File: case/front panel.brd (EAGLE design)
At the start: 165 x 30.1 mm, 3 parts

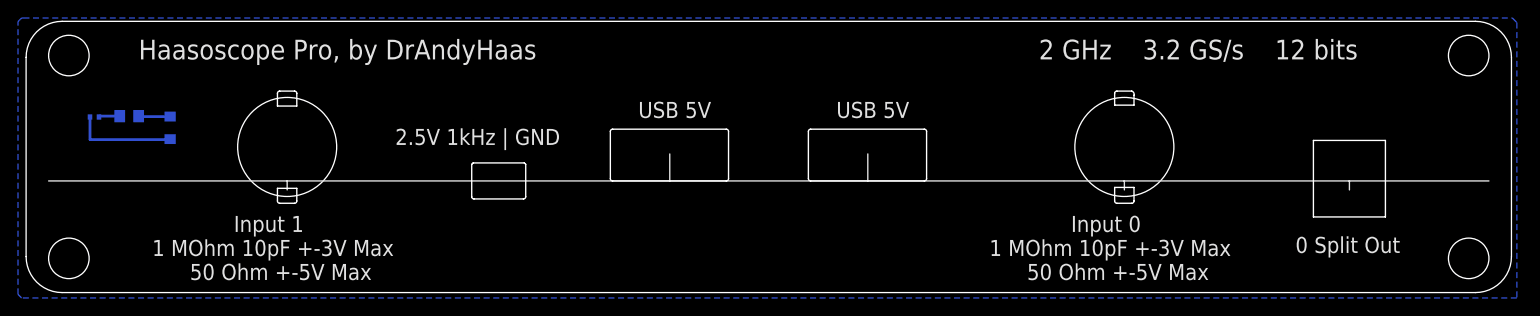
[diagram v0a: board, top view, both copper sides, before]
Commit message: add rgb leds
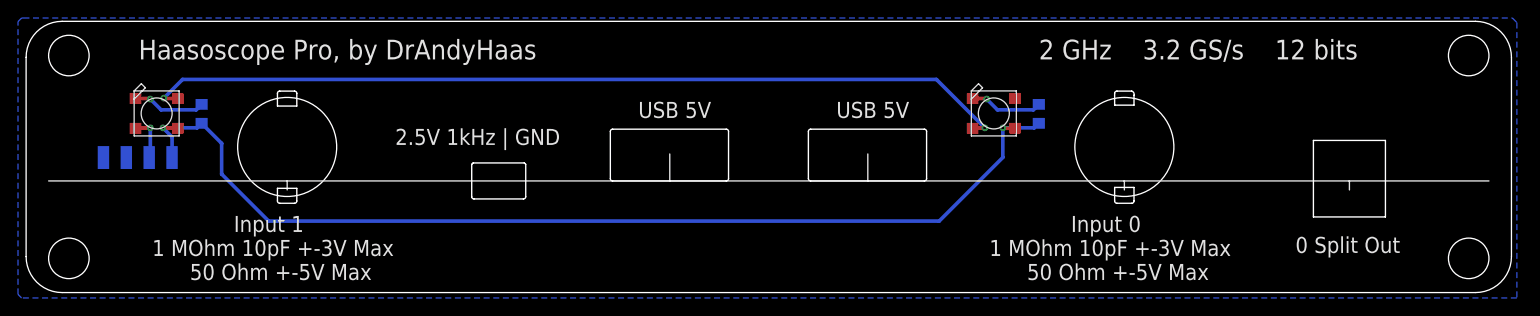
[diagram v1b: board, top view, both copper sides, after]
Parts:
- removed D2: green, MF_LEDs:LED0805
- removed R2: 3.3k, FlashPCB_Resistors:RES-0402
- added C2: 0.1uF, Nordic_nRF:RESC0805_N
- added CN1: 1X4SMT, adafruit:1X4-SMT
- added LED1, LED2: WS2812B_5050N, adafruit:WS2812B-NARROW
- C1: value 10uF -> 0.1uF
- moved C1 8.11 mm to (17.0, 20.0), turned to 90 degrees
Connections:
- new net DIN: CN1.2, LED1.4-DIN
- net 5V: now also C2.1, CN1.1, LED1.1-VDD, LED2.1-VDD; no longer D2.ANODE
- net GND: now also C2.2, CN1.3, CN1.4, LED1.3-GND, LED2.3-GND; no longer R2.P$1
- net N$2: now also LED1.2-DOUT, LED2.4-DIN; no longer D2.CATHODE, R2.P$2
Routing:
- net 5V: track 3.52 -> 117.2 mm, vias 0 -> 2
- net N$2: track 11.4 -> 97.2 mm, vias 0 -> 2
- net GND: track 2.34 -> 16.2 mm, vias 0 -> 2
- net DIN: track 0.00 -> 5.02 mm, vias 0 -> 1
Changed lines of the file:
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@@
 <drawing>
 <settings>
-<setting alwaysvectorfont="no"/>
+<setting alwaysvectorfont="yes"/>
 <setting verticaltext="up"/>
 </settings>
@@
 </autorouter>
 <elements>
-<element name="D2" library="MF_LEDs" package="LED0805" value="green" x="13.5" y="18.4" smashed="yes" rot="MR90">
-<attribute name="HOUSEPART" value="NO" x="19.9" y="15.4" size="1.778" layer="28" rot="MR90" display="off"/>
-<attribute name="MPN" value="" x="19.9" y="15.4" size="1.778" layer="28" rot="MR90" display="off"/>
-<attribute name="POPULATE" value="1" x="19.9" y="15.4" size="1.778" layer="28" rot="MR90" display="off"/>
-<attribute name="URL" value="" x="19.9" y="15.4" size="1.778" layer="28" rot="MR90" display="off"/>
-</element>
-<element name="R2" library="FlashPCB_Resistors" package="RES-0402" value="3.3k" x="5.1" y="19.6" smashed="yes" rot="MR0"/>
-<element name="C1" library="Nordic_nRF" library_urn="urn:adsk.eagle:library:169009" package="RESC0805_N" package3d_urn="urn:adsk.eagle:package:2593736/1" value="10uF" x="8.9" y="19.7" smashed="yes" rot="MR0"/>
+<element name="C1" library="Nordic_nRF" library_urn="urn:adsk.eagle:library:169009" package="RESC0805_N" package3d_urn="urn:adsk.eagle:package:2593736/1" value="0.1uF" x="17" y="20" smashed="yes" rot="MR90"/>
+<element name="LED1" library="adafruit" package="WS2812B-NARROW" value="WS2812B_5050N" x="12" y="20" smashed="yes"/>
+<element name="LED2" library="adafruit" package="WS2812B-NARROW" value="WS2812B_5050N" x="105" y="20" smashed="yes"/>
+<element name="CN1" library="adafruit" package="1X4-SMT" value="1X4SMT" x="9.9" y="15.1" smashed="yes" rot="MR0"/>
+<element name="C2" library="Nordic_nRF" library_urn="urn:adsk.eagle:library:169009" package="RESC0805_N" package3d_urn="urn:adsk.eagle:package:2593736/1" value="0.1uF" x="110" y="20" smashed="yes" rot="MR90"/>
 </elements>
 <signals>
@@
 </signal>
 <signal name="GND">
-<contactref element="R2" pad="P$1"/>
 <contactref element="C1" pad="2"/>
-<wire x1="7.9" y1="19.7" x2="5.7" y2="19.7" width="0.3048" layer="16"/>
-<wire x1="5.7" y1="19.7" x2="5.6" y2="19.6" width="0.3048" layer="16"/>
 <polygon width="0.1524" layer="16">
 <vertex x="-2.8" y="30.6"/>
@@
 <vertex x="-3" y="30.6"/>
 </polygon>
+<contactref element="LED1" pad="3-GND"/>
+<contactref element="LED2" pad="3-GND"/>
+<contactref element="CN1" pad="4"/>
+<contactref element="CN1" pad="3"/>
+<contactref element="C2" pad="2"/>
+<wire x1="102.65" y1="21.65" x2="104.15" y2="21.65" width="0.4064" layer="1"/>
+<wire x1="104.15" y1="21.65" x2="104.2" y2="21.6" width="0.4064" layer="1"/>
+<via x="104.2" y="21.6" extent="1-16" drill="0.35"/>
+<wire x1="109.4" y1="20.4" x2="105.4" y2="20.4" width="0.4064" layer="16"/>
+<wire x1="104.2" y1="21.6" x2="105.4" y2="20.4" width="0.4064" layer="16"/>
+<wire x1="110" y1="21" x2="109.4" y2="20.4" width="0.4064" layer="16"/>
+<wire x1="9.65" y1="21.65" x2="11.25" y2="21.65" width="0.4064" layer="1"/>
+<wire x1="11.25" y1="21.65" x2="11.3" y2="21.6" width="0.4064" layer="1"/>
+<via x="11.3" y="21.6" extent="1-16" drill="0.35"/>
+<wire x1="16.4" y1="20.4" x2="12.5" y2="20.4" width="0.4064" layer="16"/>
+<wire x1="11.3" y1="21.6" x2="12.5" y2="20.4" width="0.4064" layer="16"/>
+<wire x1="17" y1="21" x2="16.4" y2="20.4" width="0.4064" layer="16"/>
 </signal>
 <signal name="5V">
-<contactref element="D2" pad="ANODE"/>
 <contactref element="C1" pad="1"/>
-<wire x1="13.5" y1="19.65" x2="10.05" y2="19.65" width="0.3048" layer="16"/>
-<wire x1="10.05" y1="19.65" x2="10" y2="19.7" width="0.3048" layer="16"/>
+<contactref element="LED2" pad="1-VDD"/>
+<contactref element="LED1" pad="1-VDD"/>
+<contactref element="CN1" pad="1"/>
+<contactref element="C2" pad="1"/>
+<wire x1="14.35" y1="18.35" x2="14.3" y2="18.4" width="0.4064" layer="1"/>
+<wire x1="14.3" y1="18.4" x2="12.7" y2="18.4" width="0.4064" layer="1"/>
+<via x="12.7" y="18.4" extent="1-16" drill="0.35"/>
+<wire x1="12.7" y1="18.4" x2="13.71" y2="17.39" width="0.4064" layer="16"/>
+<wire x1="13.71" y1="17.39" x2="13.71" y2="15.1" width="0.4064" layer="16"/>
+<wire x1="12.7" y1="18.4" x2="16.5" y2="18.4" width="0.4064" layer="16"/>
+<wire x1="16.5" y1="18.4" x2="17" y2="18.9" width="0.4064" layer="16"/>
+<wire x1="17" y1="18.9" x2="19.222" y2="16.678" width="0.4064" layer="16"/>
+<wire x1="19.222" y1="16.678" x2="19.222" y2="13.26034375" width="0.4064" layer="16"/>
+<wire x1="19.222" y1="13.26034375" x2="24.44114375" y2="8.0412" width="0.4064" layer="16"/>
+<wire x1="24.44114375" y1="8.0412" x2="98.93146875" y2="8.0412" width="0.4064" layer="16"/>
+<wire x1="110" y1="18.9" x2="109.5" y2="18.4" width="0.4064" layer="16"/>
+<wire x1="109.5" y1="18.4" x2="106" y2="18.4" width="0.4064" layer="16"/>
+<via x="106" y="18.4" extent="1-16" drill="0.35"/>
+<wire x1="107.35" y1="18.35" x2="106.05" y2="18.35" width="0.4064" layer="1"/>
+<wire x1="106.05" y1="18.35" x2="106" y2="18.4" width="0.4064" layer="1"/>
+<wire x1="106" y1="15.10973125" x2="106" y2="18.4" width="0.4064" layer="16"/>
+<wire x1="98.93146875" y1="8.0412" x2="106" y2="15.10973125" width="0.4064" layer="16"/>
 </signal>
 <signal name="N$2">
-<contactref element="R2" pad="P$2"/>
-<contactref element="D2" pad="CATHODE"/>
-<wire x1="4.6" y1="19.6" x2="4.6" y2="17.1" width="0.3048" layer="16"/>
-<wire x1="4.6" y1="17.1" x2="13.45" y2="17.1" width="0.3048" layer="16"/>
-<wire x1="13.45" y1="17.1" x2="13.5" y2="17.15" width="0.3048" layer="16"/>
+<contactref element="LED1" pad="2-DOUT"/>
+<contactref element="LED2" pad="4-DIN"/>
+<wire x1="14.35" y1="21.65" x2="12.85" y2="21.65" width="0.4064" layer="1"/>
+<wire x1="12.85" y1="21.65" x2="12.8" y2="21.7" width="0.4064" layer="1"/>
+<via x="12.8" y="21.7" extent="1-16" drill="0.35"/>
+<via x="104" y="18.4" extent="1-16" drill="0.35"/>
+<wire x1="98.6246" y1="23.7754" x2="14.8754" y2="23.7754" width="0.4064" layer="16"/>
+<wire x1="12.8" y1="21.7" x2="14.8754" y2="23.7754" width="0.4064" layer="16"/>
+<wire x1="98.6246" y1="23.7754" x2="104" y2="18.4" width="0.4064" layer="16"/>
+<wire x1="104" y1="18.4" x2="102.7" y2="18.4" width="0.4064" layer="1"/>
+<wire x1="102.65" y1="18.35" x2="102.7" y2="18.4" width="0.4064" layer="1"/>
+</signal>
+<signal name="DIN">
+<contactref element="CN1" pad="2"/>
+<contactref element="LED1" pad="4-DIN"/>
+<wire x1="11.3" y1="18.4" x2="9.7" y2="18.4" width="0.4064" layer="1"/>
+<wire x1="9.65" y1="18.35" x2="9.7" y2="18.4" width="0.4064" layer="1"/>
+<via x="11.3" y="18.4" extent="1-16" drill="0.35"/>
+<wire x1="11.3" y1="18.4" x2="11.3" y2="15.23" width="0.4064" layer="16"/>
+<wire x1="11.17" y1="15.1" x2="11.3" y2="15.23" width="0.4064" layer="16"/>
 </signal>
 </signals>

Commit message: use SK6812MINI-E leds
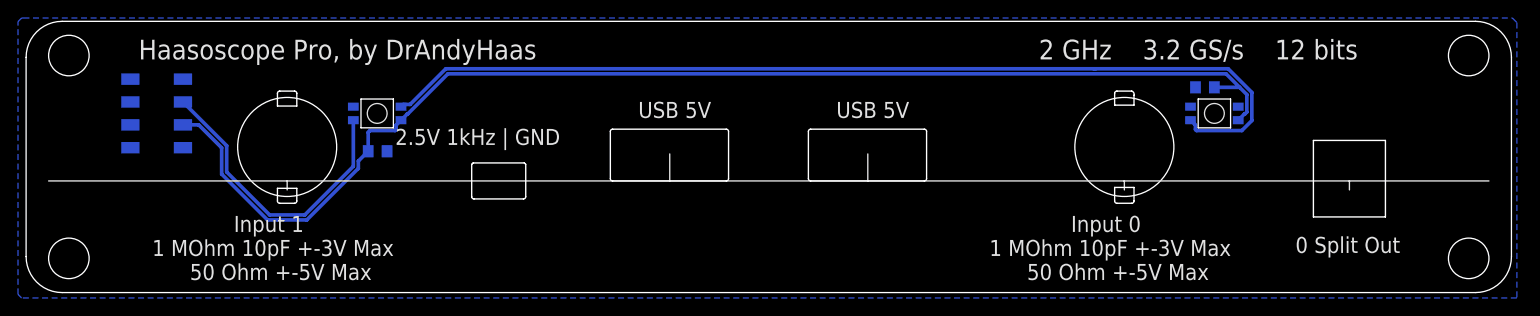
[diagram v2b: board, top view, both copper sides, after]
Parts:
- removed CN1: 1X4SMT, adafruit:1X4-SMT
- removed LED2: WS2812B_5050N, adafruit:WS2812B-NARROW
- added JP1: connect, pinhead+:2X04_SMT
- added LED0: WS2812B_SK6812E, microbuilder:NEO3535_REVERSE
- LED1: value WS2812B_5050N -> WS2812B_SK6812E; device adafruit:WS2812B-NARROW -> microbuilder:NEO3535_REVERSE
- moved LED1 24.5 mm to (36.5, 20.0)
- moved C1 20.0 mm to (36.6, 15.8), turned to 180 degrees
- moved C2 18.6 mm to (128.4, 22.9), turned to 0 degrees
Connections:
- net 5V: now also JP1.5, LED0.1-VDD; no longer CN1.1, LED2.1-VDD
- net DIN: now also JP1.3; no longer CN1.2
- net GND: now also JP1.1, JP1.2, JP1.4, JP1.6, JP1.7, JP1.8, LED0.3-GND; no longer CN1.3, CN1.4, LED2.3-GND
- net N$2: now also LED0.4-DIN; no longer LED2.4-DIN
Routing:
- net DIN: track 5.02 -> 33.2 mm, vias 1 -> 0
- net 5V: track 117.2 -> 140.0 mm, vias 2 -> 0
- net GND: track 16.2 -> 0.00 mm, vias 2 -> 0
- net N$2: track 97.2 -> 108.5 mm, vias 2 -> 0
